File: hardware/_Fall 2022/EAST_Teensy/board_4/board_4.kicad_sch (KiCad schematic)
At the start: 10 parts, among them J1 Conn_01x04, U1 Teensy4.1

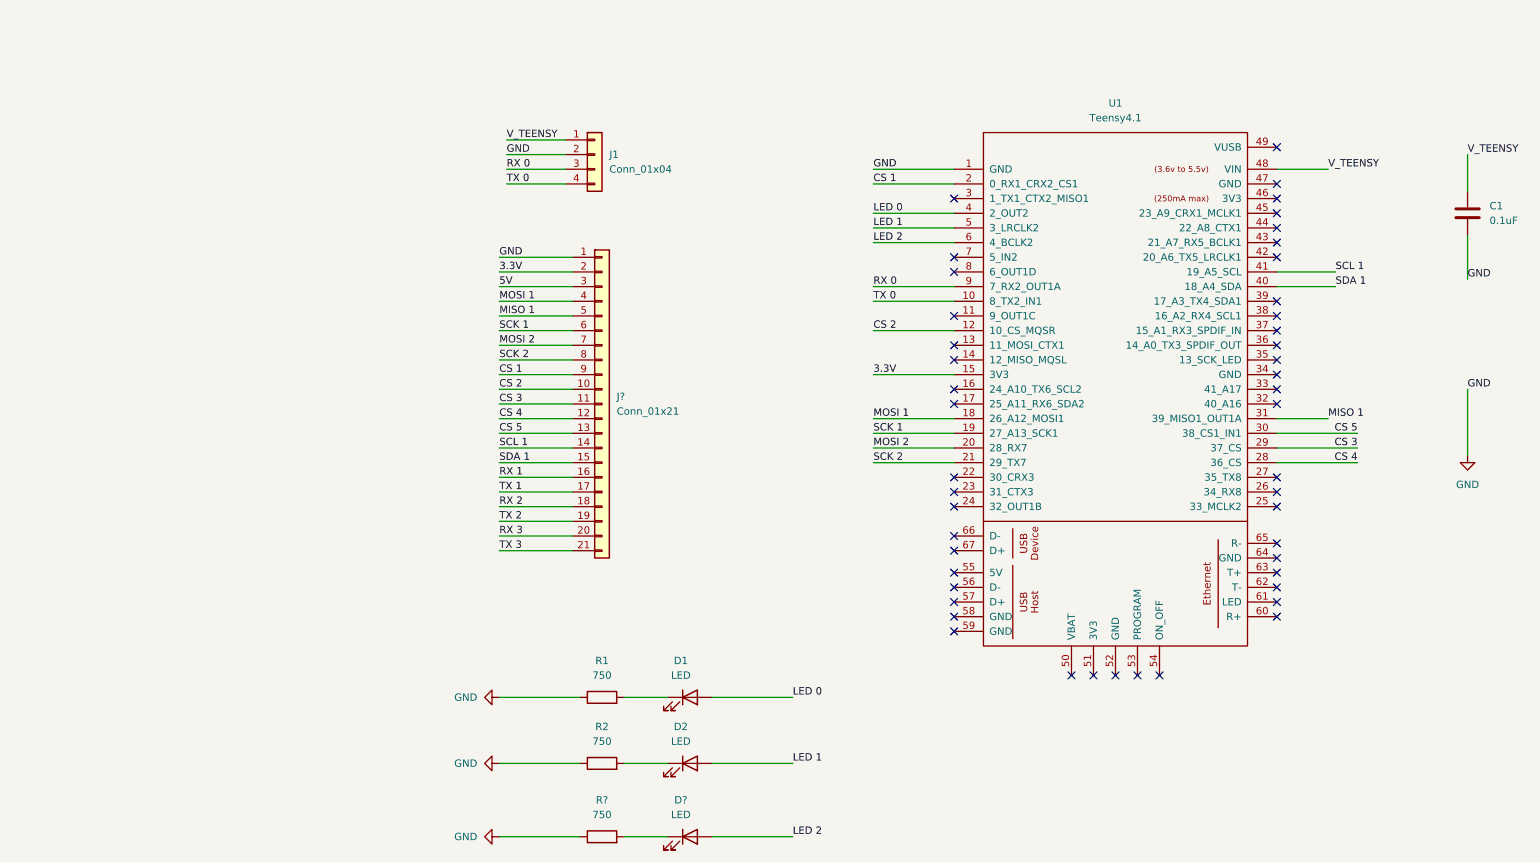
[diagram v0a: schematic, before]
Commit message: Add buzzer and take out 2nd SPI
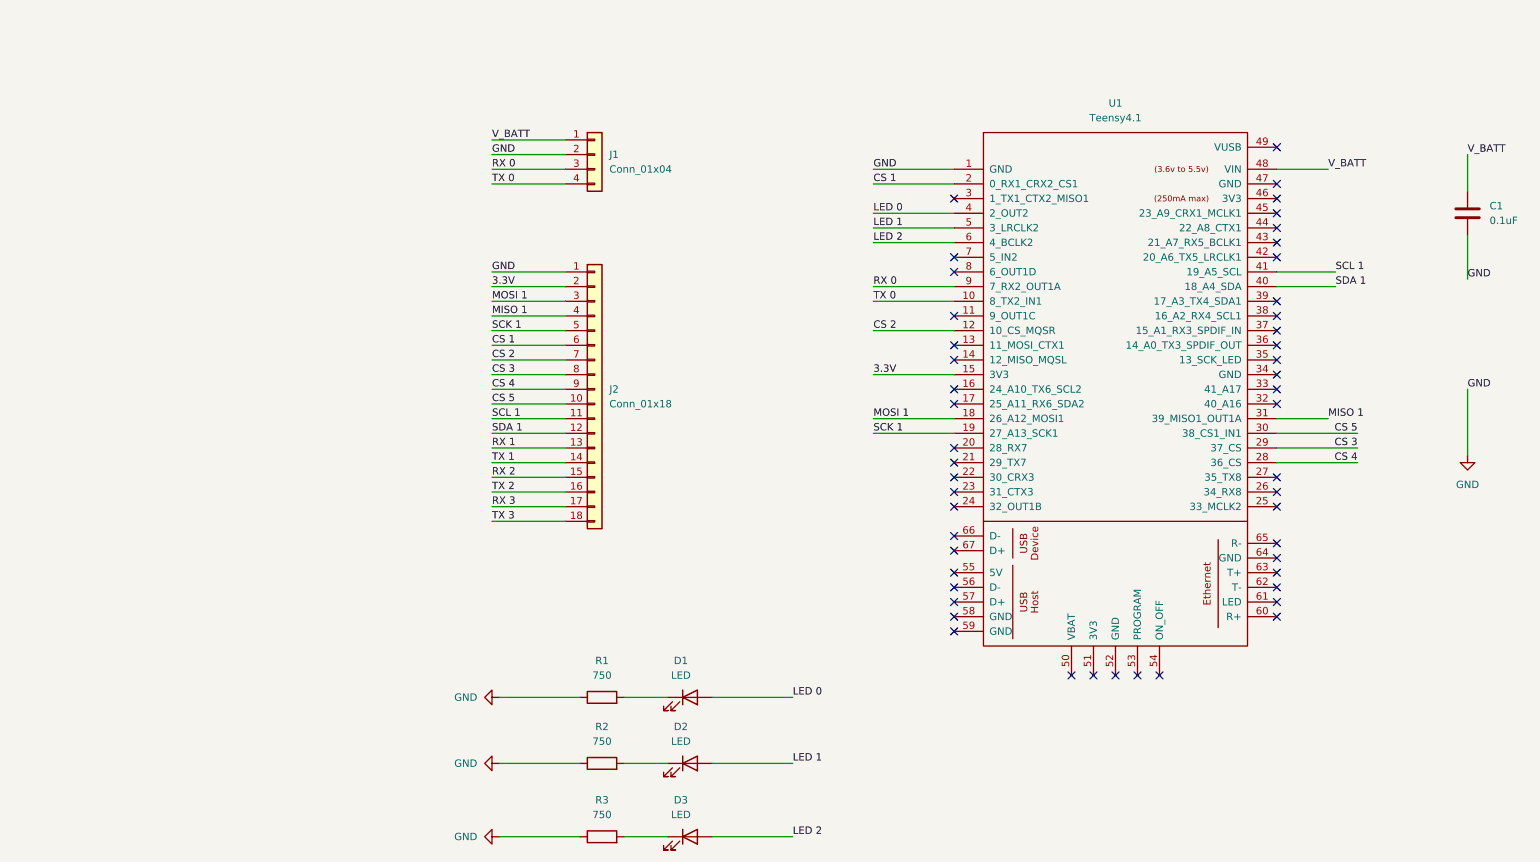
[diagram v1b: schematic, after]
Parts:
- removed J?: Conn_01x21, symbol Connector_Generic:Conn_01x21
- added J2: Conn_01x18, symbol Connector_Generic:Conn_01x18
- gave numbers to parts that had none: 2
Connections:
- net 3.3V: now also J2.2 (Pin_2)
- net CS 1: now also J2.6 (Pin_6)
- net CS 2: now also J2.7 (Pin_7)
- net CS 3: now also J2.8 (Pin_8)
- net CS 4: now also J2.9 (Pin_9)
- net CS 5: now also J2.10 (Pin_10)
- net GND: now also J2.1 (Pin_1)
- net MISO 1: now also J2.4 (Pin_4)
- net MOSI 1: now also J2.3 (Pin_3)
- net RX 1: now also J2.13 (Pin_13)
- net RX 2: now also J2.15 (Pin_15)
- net RX 3: now also J2.17 (Pin_17)
- net SCK 1: now also J2.5 (Pin_5)
- net SCL 1: now also J2.11 (Pin_11)
- net SDA 1: now also J2.12 (Pin_12)
- net TX 1: now also J2.14 (Pin_14)
- net TX 2: now also J2.16 (Pin_16)
- net TX 3: now also J2.18 (Pin_18)
- net MOSI 2: no longer names the net of U1.20 (28_RX7)
- net SCK 2: no longer names the net of U1.21 (29_TX7)
- net V_TEENSY renamed V_BATT
- no-connect marks 47 -> 49

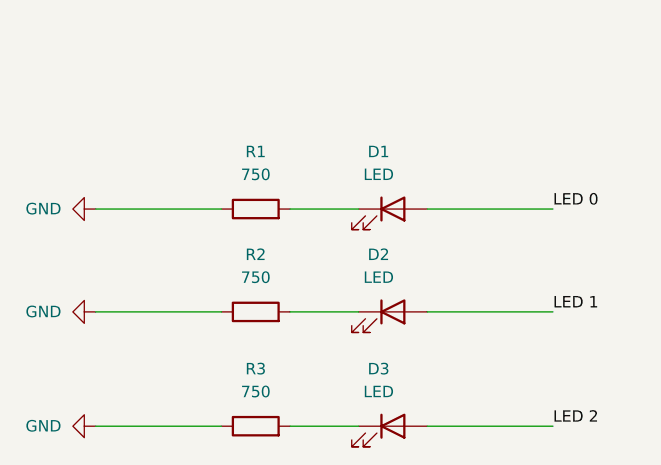
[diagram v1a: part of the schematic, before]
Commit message: Add footprints to resistors and LEDs
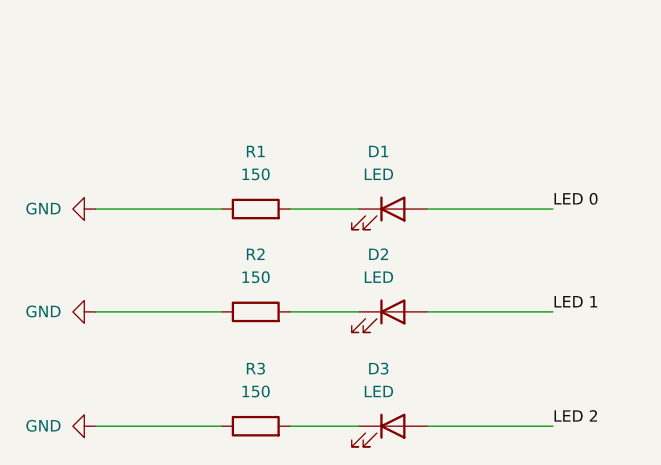
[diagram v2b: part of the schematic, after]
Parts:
- C1: footprint (none) -> Capacitor_SMD:C_0805_2012Metric_Pad1.18x1.45mm_HandSolder
- D1, D2, D3: footprint (none) -> LED_SMD:LED_0805_2012Metric_Pad1.15x1.40mm_HandSolder
- J1: footprint (none) -> Connector_JST:JST_PH_S4B-PH-K_1x04_P2.00mm_Horizontal
- R1, R2, R3: value 750 -> 150; footprint (none) -> Resistor_SMD:R_0805_2012Metric_Pad1.20x1.40mm_HandSolder
- U1: footprint (none) -> Teensy:Teensy41
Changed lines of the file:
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@@
     (in_bom yes) (on_board yes) (fields_autoplaced)
     (property "Reference" "R2" (id 0) (at 114.3 135.89 90))
-    (property "Value" "750" (id 1) (at 114.3 138.43 90))
-    (property "Footprint" "" (id 2) (at 114.3 144.018 90)
+    (property "Value" "150" (id 1) (at 114.3 138.43 90))
+    (property "Footprint" "Resistor_SMD:R_0805_2012Metric_Pad1.20x1.40mm_HandSolder" (id 2) (at 114.3 144.018 90)
       (effects (font (size 1.27 1.27)) hide)
     )
@@
       (effects (font (size 1.27 1.27)) (justify left))
     )
-    (property "Footprint" "" (id 2) (at 265.1252 50.8 0)
+    (property "Footprint" "Capacitor_SMD:C_0805_2012Metric_Pad1.18x1.45mm_HandSolder" (id 2) (at 265.1252 50.8 0)
       (effects (font (size 1.27 1.27)) hide)
     )
@@
     (in_bom yes) (on_board yes) (fields_autoplaced)
     (property "Reference" "R3" (id 0) (at 114.3 148.59 90))
-    (property "Value" "750" (id 1) (at 114.3 151.13 90))
-    (property "Footprint" "" (id 2) (at 114.3 156.718 90)
+    (property "Value" "150" (id 1) (at 114.3 151.13 90))
+    (property "Footprint" "Resistor_SMD:R_0805_2012Metric_Pad1.20x1.40mm_HandSolder" (id 2) (at 114.3 156.718 90)
       (effects (font (size 1.27 1.27)) hide)
     )
@@
     (property "Reference" "D2" (id 0) (at 127.9525 135.89 0))
     (property "Value" "LED" (id 1) (at 127.9525 138.43 0))
-    (property "Footprint" "" (id 2) (at 129.54 142.24 0)
-      (effects (font (size 1.27 1.27)) hide)
-    )
-    (property "Datasheet" "~" (id 3) (at 129.54 142.24 0)
+    (property "Footprint" "LED_SMD:LED_0805_2012Metric_Pad1.15x1.40mm_HandSolder" (id 2) (at 129.54 142.24 0)
+      (effects (font (size 1.27 1.27)) hide)
+    )
+    (property "Datasheet" "https://datasheet.lcsc.com/lcsc/1806130620_Hubei-KENTO-Elec-C2293_C2293.pdf" (id 3) (at 129.54 142.24 0)
       (effects (font (size 1.27 1.27)) hide)
     )
@@
     (property "Reference" "U1" (id 0) (at 203.2 27.94 0))
     (property "Value" "Teensy4.1" (id 1) (at 203.2 30.48 0))
-    (property "Footprint" "" (id 2) (at 193.04 83.82 0)
+    (property "Footprint" "Teensy:Teensy41" (id 2) (at 193.04 83.82 0)
       (effects (font (size 1.27 1.27)) hide)
     )
@@
     (property "Reference" "D1" (id 0) (at 127.9525 124.46 0))
     (property "Value" "LED" (id 1) (at 127.9525 127 0))
-    (property "Footprint" "" (id 2) (at 129.54 130.81 0)
-      (effects (font (size 1.27 1.27)) hide)
-    )
-    (property "Datasheet" "~" (id 3) (at 129.54 130.81 0)
+    (property "Footprint" "LED_SMD:LED_0805_2012Metric_Pad1.15x1.40mm_HandSolder" (id 2) (at 129.54 130.81 0)
+      (effects (font (size 1.27 1.27)) hide)
+    )
+    (property "Datasheet" "https://datasheet.lcsc.com/lcsc/1806130620_Hubei-KENTO-Elec-C2293_C2293.pdf" (id 3) (at 129.54 130.81 0)
       (effects (font (size 1.27 1.27)) hide)
     )
@@
     (in_bom yes) (on_board yes) (fields_autoplaced)
     (property "Reference" "R1" (id 0) (at 114.3 124.46 90))
-    (property "Value" "750" (id 1) (at 114.3 127 90))
-    (property "Footprint" "" (id 2) (at 114.3 132.588 90)
+    (property "Value" "150" (id 1) (at 114.3 127 90))
+    (property "Footprint" "Resistor_SMD:R_0805_2012Metric_Pad1.20x1.40mm_HandSolder" (id 2) (at 114.3 132.588 90)
       (effects (font (size 1.27 1.27)) hide)
     )
@@
     (property "Reference" "D3" (id 0) (at 127.9525 148.59 0))
     (property "Value" "LED" (id 1) (at 127.9525 151.13 0))
-    (property "Footprint" "" (id 2) (at 129.54 154.94 0)
-      (effects (font (size 1.27 1.27)) hide)
-    )
-    (property "Datasheet" "~" (id 3) (at 129.54 154.94 0)
+    (property "Footprint" "LED_SMD:LED_0805_2012Metric_Pad1.15x1.40mm_HandSolder" (id 2) (at 129.54 154.94 0)
+      (effects (font (size 1.27 1.27)) hide)
+    )
+    (property "Datasheet" "https://datasheet.lcsc.com/lcsc/1806130620_Hubei-KENTO-Elec-C2293_C2293.pdf" (id 3) (at 129.54 154.94 0)
       (effects (font (size 1.27 1.27)) hide)
     )
@@
       (effects (font (size 1.27 1.27)) (justify left))
     )
-    (property "Footprint" "" (id 2) (at 113.03 36.83 0)
+    (property "Footprint" "Connector_JST:JST_PH_S4B-PH-K_1x04_P2.00mm_Horizontal" (id 2) (at 113.03 36.83 0)
       (effects (font (size 1.27 1.27)) hide)
     )
@@
     )
     (path "/82e280a4-56a4-4b9c-912d-48b78e5c2f29"
-      (reference "C1") (unit 1) (value "0.1uF") (footprint "")
+      (reference "C1") (unit 1) (value "0.1uF") (footprint "Capacitor_SMD:C_0805_2012Metric_Pad1.18x1.45mm_HandSolder")
     )
     (path "/bacf17dc-6113-4272-9cec-ac932b008691"
-      (reference "D1") (unit 1) (value "LED") (footprint "")
+      (reference "D1") (unit 1) (value "LED") (footprint "LED_SMD:LED_0805_2012Metric_Pad1.15x1.40mm_HandSolder")
     )
     (path "/adf90281-4711-4510-9131-65a6deeda189"
-      (reference "D2") (unit 1) (value "LED") (footprint "")
+      (reference "D2") (unit 1) (value "LED") (footprint "LED_SMD:LED_0805_2012Metric_Pad1.15x1.40mm_HandSolder")
     )
     (path "/eb0265a4-502c-4abe-80cd-5ef54c8c8a3b"
-      (reference "D3") (unit 1) (value "LED") (footprint "")
+      (reference "D3") (unit 1) (value "LED") (footprint "LED_SMD:LED_0805_2012Metric_Pad1.15x1.40mm_HandSolder")
     )
     (path "/f852b861-1da2-4c35-8389-6db74b76175d"
-      (reference "J1") (unit 1) (value "Conn_01x04") (footprint "")
+      (reference "J1") (unit 1) (value "Conn_01x04") (footprint "Connector_JST:JST_PH_S4B-PH-K_1x04_P2.00mm_Horizontal")
     )
     (path "/cd6d8097-444b-4639-a32d-b99ac13e9730"
@@
     )
     (path "/e655f3b3-e993-4244-95f7-b84bf5f4db23"
-      (reference "R1") (unit 1) (value "750") (footprint "")
+      (reference "R1") (unit 1) (value "150") (footprint "Resistor_SMD:R_0805_2012Metric_Pad1.20x1.40mm_HandSolder")
     )
     (path "/5af9e313-f930-4ec8-8beb-eefb401bc19d"
-      (reference "R2") (unit 1) (value "750") (footprint "")
+      (reference "R2") (unit 1) (value "150") (footprint "Resistor_SMD:R_0805_2012Metric_Pad1.20x1.40mm_HandSolder")
     )
     (path "/97742eef-9c26-48d1-9ae0-0474ed59d1e4"
-      (reference "R3") (unit 1) (value "750") (footprint "")
+      (reference "R3") (unit 1) (value "150") (footprint "Resistor_SMD:R_0805_2012Metric_Pad1.20x1.40mm_HandSolder")
     )
     (path "/b2758a0a-4bfb-4a9e-9bf3-46b060736299"
-      (reference "U1") (unit 1) (value "Teensy4.1") (footprint "")
-    )
-  )
+      (reference "U1") (unit 1) (value "Teensy4.1") (footprint "Teensy:Teensy41")
+    )
+  )

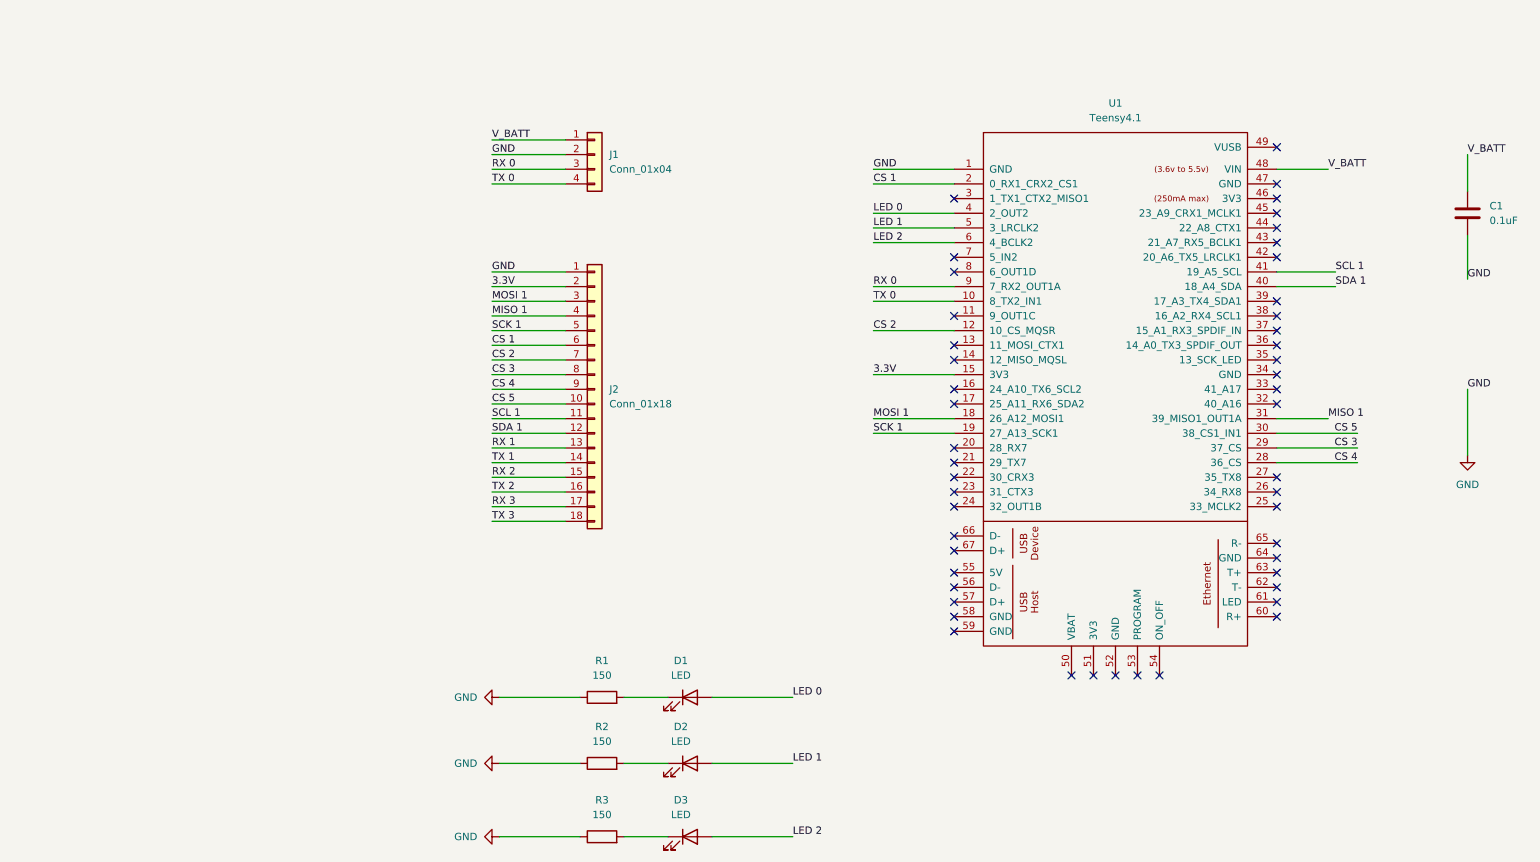
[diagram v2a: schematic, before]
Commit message: Add east teensy footprint
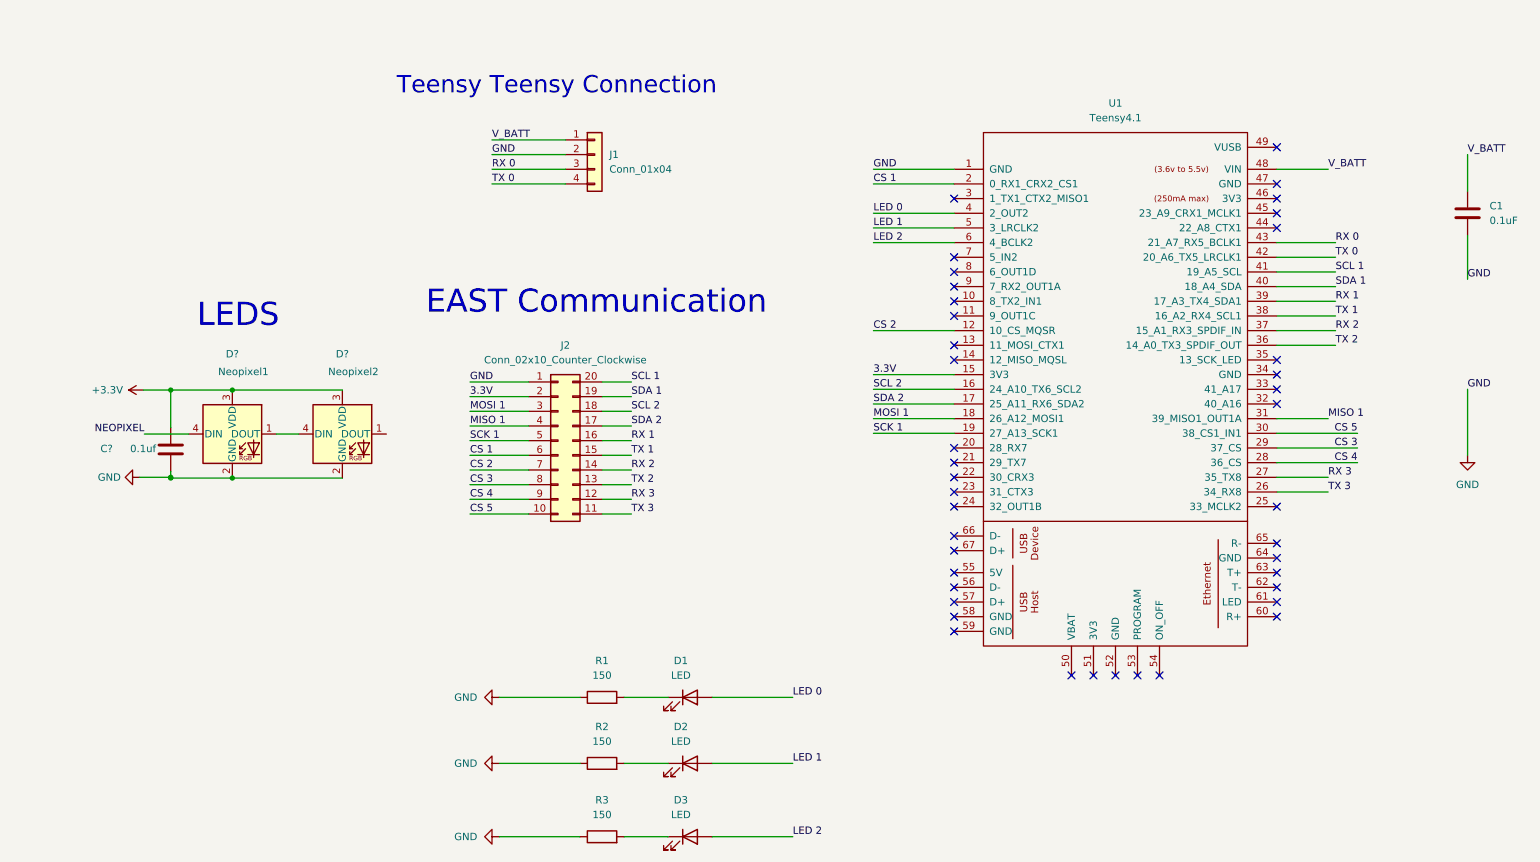
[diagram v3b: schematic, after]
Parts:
- removed J2: Conn_01x18, symbol Connector_Generic:Conn_01x18
- added C?: 0.1uf, Capacitor_Tantalum_SMD:CP_EIA-1608-08_AVX-J, symbol Device:C
- added D?: Neopixel1, neopixel:LED_1655, symbol LED:NeoPixel_THT
- added D?: Neopixel2, neopixel:LED_1655, symbol LED:NeoPixel_THT
- added J2: Conn_02x10_Counter_Clockwise, Connector_PinHeader_2.54mm:PinHeader_2x10_P2.54mm_Vertical, symbol Connector_Generic:Conn_02x10_Counter_Clockwise
- C1: footprint Capacitor_SMD:C_0805_2012Metric_Pad1.18x1.45mm_HandSolder -> Capacitor_SMD:C_0201_0603Metric
- D1, D2, D3: footprint LED_SMD:LED_0805_2012Metric_Pad1.15x1.40mm_HandSolder -> LED_SMD:LED_0201_0603Metric
- R1, R2, R3: footprint Resistor_SMD:R_0805_2012Metric_Pad1.20x1.40mm_HandSolder -> Resistor_SMD:R_0201_0603Metric
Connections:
- net 3.3V: now also J2.2 (Pin_2)
- net CS 1: now also J2.6 (Pin_6)
- net CS 2: now also J2.7 (Pin_7)
- net CS 3: now also J2.8 (Pin_8)
- net CS 4: now also J2.9 (Pin_9)
- net CS 5: now also J2.10 (Pin_10)
- net GND: now also C?.1, D?.2 (GND), D?.2 (GND), J2.1 (Pin_1)
- net MISO 1: now also J2.4 (Pin_4)
- net MOSI 1: now also J2.3 (Pin_3)
- net RX 0: now also U1.43 (21_A7_RX5_BCLK1); no longer U1.9 (7_RX2_OUT1A)
- net RX 1: now also U1.39 (17_A3_TX4_SDA1), J2.16 (Pin_16)
- net RX 2: now also U1.37 (15_A1_RX3_SPDIF_IN), J2.14 (Pin_14)
- net RX 3: now also U1.27 (35_TX8), J2.12 (Pin_12)
- net SCK 1: now also J2.5 (Pin_5)
- net SCL 1: now also J2.20 (Pin_20)
- net SDA 1: now also J2.19 (Pin_19)
- net TX 0: now also U1.42 (20_A6_TX5_LRCLK1); no longer U1.10 (8_TX2_IN1)
- net TX 1: now also U1.38 (16_A2_RX4_SCL1), J2.15 (Pin_15)
- net TX 2: now also U1.36 (14_A0_TX3_SPDIF_OUT), J2.13 (Pin_13)
- net TX 3: now also U1.26 (34_RX8), J2.11 (Pin_11)
- net SCL 2: now reaches U1.16 (24_A10_TX6_SCL2)
- net SCL 2: now also J2.18 (Pin_18)
- net SDA 2: now reaches U1.17 (25_A11_RX6_SDA2)
- net SDA 2: now also J2.17 (Pin_17)
- new net: D?.1 (DOUT), D?.4 (DIN)
- new net +3.3V: C?.2, D?.3 (VDD), D?.3 (VDD)
- new net NEOPIXEL: D?.4 (DIN)
- no-connect marks 49 -> 41
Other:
- note added: "EAST Communication"
- note added: "LEDS"
- note added: "Teensy Teensy Connection"
